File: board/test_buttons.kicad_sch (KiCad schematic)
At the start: 0 parts

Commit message: Added Parts, Renamed Parts
Added in switches, buttons, & multiple anderson connections for power.
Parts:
- added SW1, SW2, SW3: SW_Push, symbol Switch:SW_Push
- added SW4: SW_SPDT, symbol Switch:SW_SPDT
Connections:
- new net +3.3V: SW4.1 (A)
- new net Dir_Switch: SW4.2 (B)
- new net GND: SW1.2, SW2.2, SW3.2, SW4.3 (C)
- new net SW1: SW1.1
- new net SW2: SW2.1
- new net SW3: SW3.1

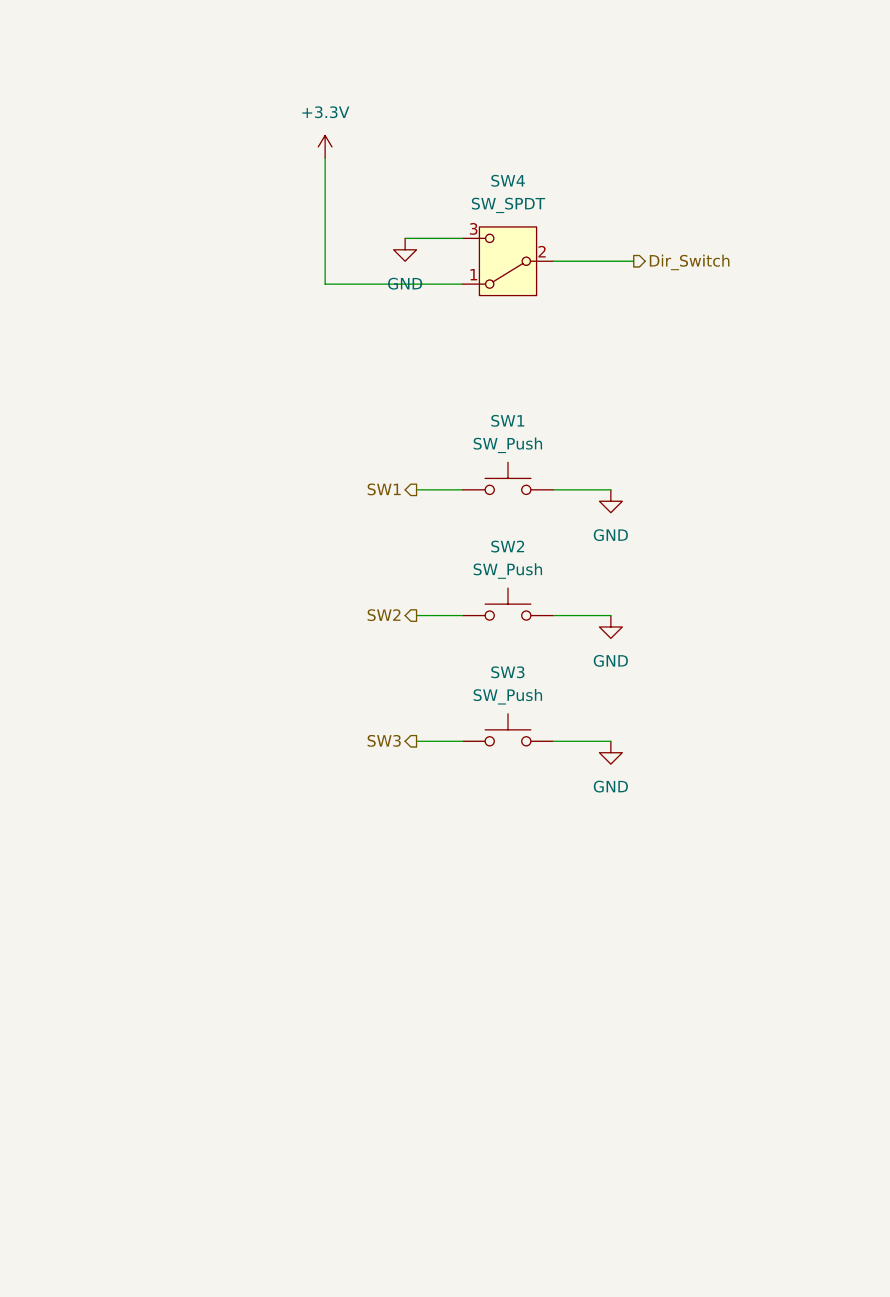
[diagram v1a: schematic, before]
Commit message: Added Labels, Missing Requirements, and Refined Look
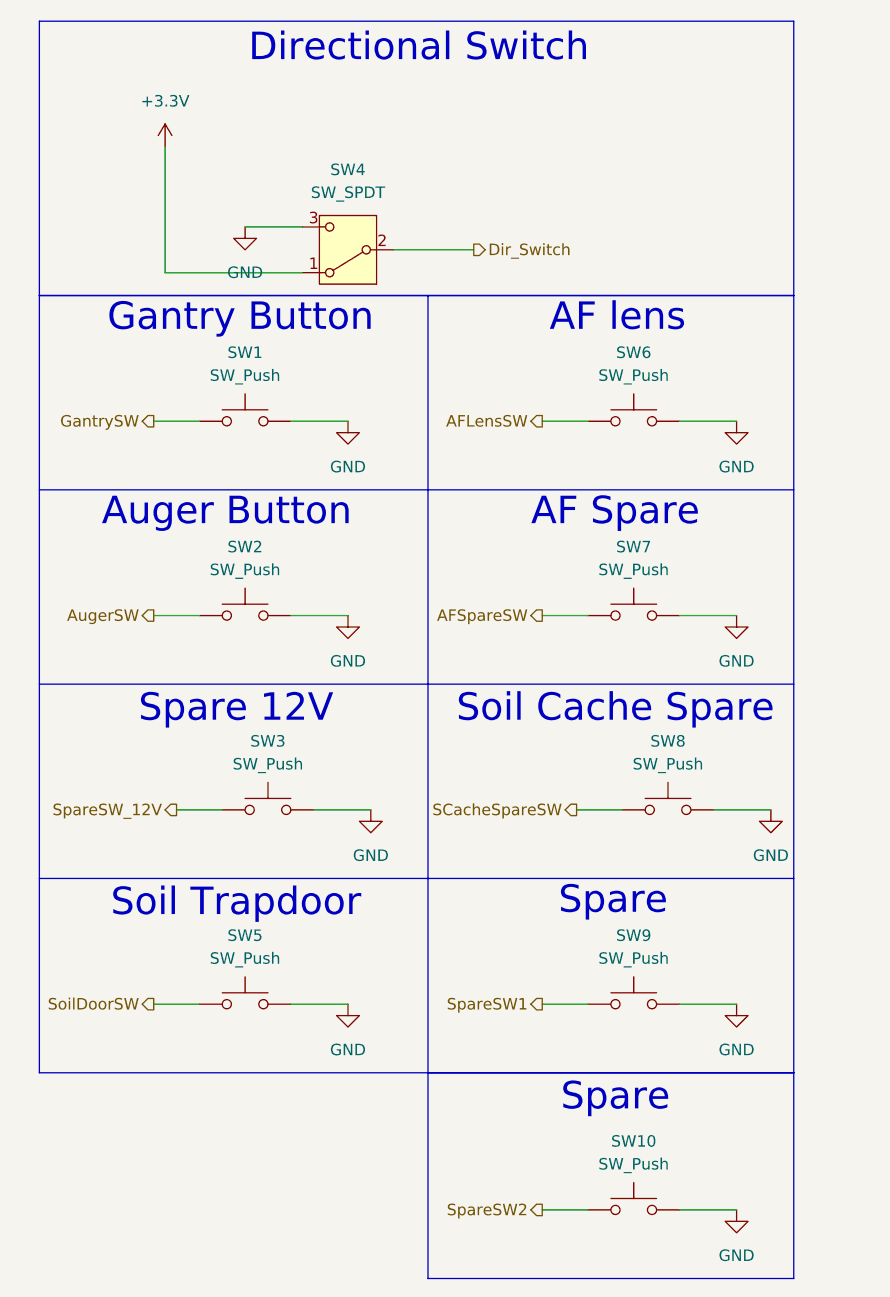
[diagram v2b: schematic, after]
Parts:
- added SW10, SW5, SW6, SW7, SW8, SW9: SW_Push, symbol Switch:SW_Push
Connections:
- net GND: now also SW10.2, SW5.2, SW6.2, SW7.2, SW8.2, SW9.2
- net SW1 renamed GantrySW
- net SW2 renamed AugerSW
- net SW3 renamed SpareSW_12V
- new net AFLensSW: SW6.1
- new net AFSpareSW: SW7.1
- new net SCacheSpareSW: SW8.1
- new net SoilDoorSW: SW5.1
- new net SpareSW1: SW9.1
- new net SpareSW2: SW10.1
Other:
- note added: "AF Spare"
- note added: "AF lens"
- note added: "Auger Button"
- note added: "Directional Switch"
- note added: "Gantry Button"
- note added: "Soil Cache Spare"
- note added: "Soil Trapdoor"
- note added: "Spare"
- note added: "Spare 12V"
- moved on the sheet: SW1, SW2, SW3, SW4

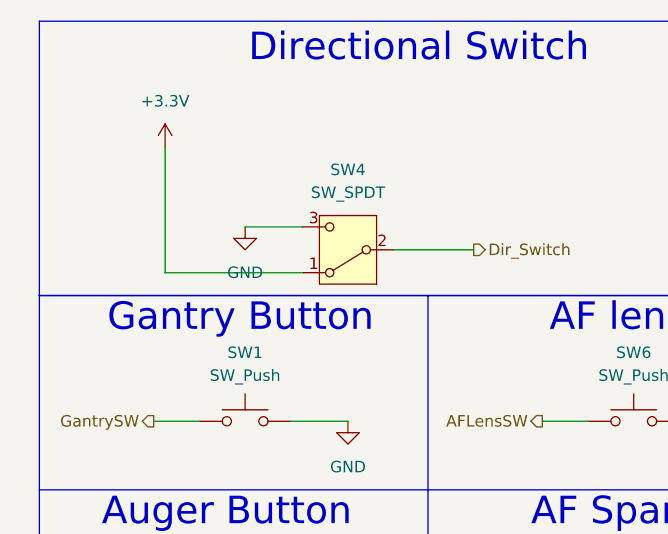
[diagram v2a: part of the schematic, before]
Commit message: Adjusted resistor values & renamed AF outputs
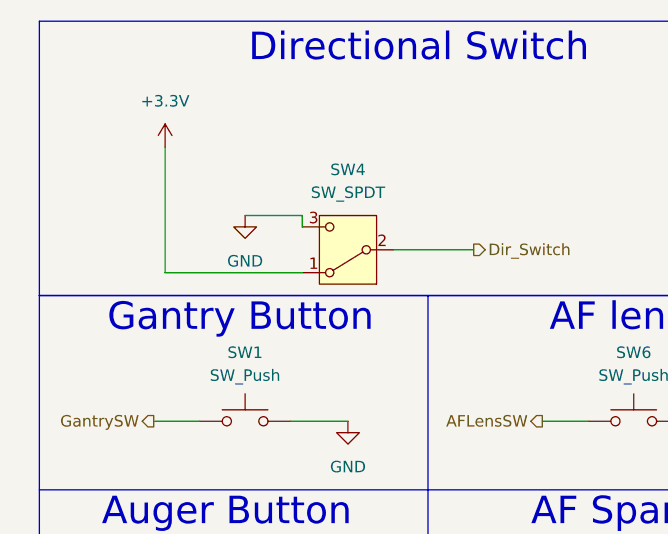
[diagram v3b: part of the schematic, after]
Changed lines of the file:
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@@
+	(wire
+		(pts
+			(xy 41.91 34.29) (xy 41.91 35.56)
+		)
+		(stroke
+			(width 0)
+			(type default)
+		)
+	)
 	(wire
 		(pts
@@
 	(wire
 		(pts
-			(xy 35.56 35.56) (xy 41.91 35.56)
+			(xy 35.56 34.29) (xy 41.91 34.29)
 		)
 		(stroke
@@
 	(symbol
 		(lib_id "power:GND")
-		(at 35.56 35.56 0)
+		(at 35.56 34.29 0)
 		(unit 1)
 		(exclude_from_sim no)
@@
 		(fields_autoplaced yes)
 		(property "Reference" "#PWR028"
-			(at 35.56 41.91 0)
+			(at 35.56 40.64 0)
 			(effects
 				(font
@@
 		)
 		(property "Value" "GND"
-			(at 35.56 40.64 0)
-			(effects
-				(font
-					(size 1.27 1.27)
-				)
-			)
-		)
-		(property "Footprint" ""
-			(at 35.56 35.56 0)
+			(at 35.56 39.37 0)
+			(effects
+				(font
+					(size 1.27 1.27)
+				)
+			)
+		)
+		(property "Footprint" ""
+			(at 35.56 34.29 0)
 			(effects
 				(font
@@
 		)
 		(property "Datasheet" ""
-			(at 35.56 35.56 0)
+			(at 35.56 34.29 0)
 			(effects
 				(font
@@
 		)
 		(property "Description" "Power symbol creates a global label with name \"GND\" , ground"
-			(at 35.56 35.56 0)
-			(effects
-				(font
+			(at 35.56 34.29 0)
+			(effects
+				(font

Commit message: assigned footprints
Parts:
- SW1, SW10, SW2, SW3, SW5, SW6, SW7, SW8, SW9: footprint (none) -> Button_Switch_SMD:SW_SPST_TL3305A
- SW4: footprint (none) -> Button_Switch_THT:SW_Slide_SPDT_Straight_CK_OS102011MS2Q
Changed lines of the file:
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@@
 			)
 		)
-		(property "Footprint" ""
+		(property "Footprint" "Button_Switch_SMD:SW_SPST_TL3305A"
 			(at 35.56 116.84 0)
 			(effects
@@
 			)
 		)
-		(property "Footprint" ""
+		(property "Footprint" "Button_Switch_SMD:SW_SPST_TL3305A"
 			(at 78.74 52.07 0)
 			(effects
@@
 			)
 		)
-		(property "Footprint" ""
+		(property "Footprint" "Button_Switch_SMD:SW_SPST_TL3305A"
 			(at 35.56 73.66 0)
 			(effects
@@
 			)
 		)
-		(property "Footprint" ""
+		(property "Footprint" "Button_Switch_SMD:SW_SPST_TL3305A"
 			(at 78.74 139.7 0)
 			(effects
@@
 			)
 		)
-		(property "Footprint" ""
+		(property "Footprint" "Button_Switch_SMD:SW_SPST_TL3305A"
 			(at 78.74 116.84 0)
 			(effects
@@
 			)
 		)
-		(property "Footprint" ""
+		(property "Footprint" "Button_Switch_SMD:SW_SPST_TL3305A"
 			(at 35.56 52.07 0)
 			(effects
@@
 			)
 		)
-		(property "Footprint" ""
+		(property "Footprint" "Button_Switch_SMD:SW_SPST_TL3305A"
 			(at 38.1 95.25 0)
 			(effects
@@
 			)
 		)
-		(property "Footprint" ""
+		(property "Footprint" "Button_Switch_THT:SW_Slide_SPDT_Straight_CK_OS102011MS2Q"
 			(at 46.99 38.1 0)
 			(effects
@@
 			)
 		)
-		(property "Footprint" ""
+		(property "Footprint" "Button_Switch_SMD:SW_SPST_TL3305A"
 			(at 78.74 73.66 0)
 			(effects
@@
 			)
 		)
-		(property "Footprint" ""
+		(property "Footprint" "Button_Switch_SMD:SW_SPST_TL3305A"
 			(at 82.55 95.25 0)
 			(effects

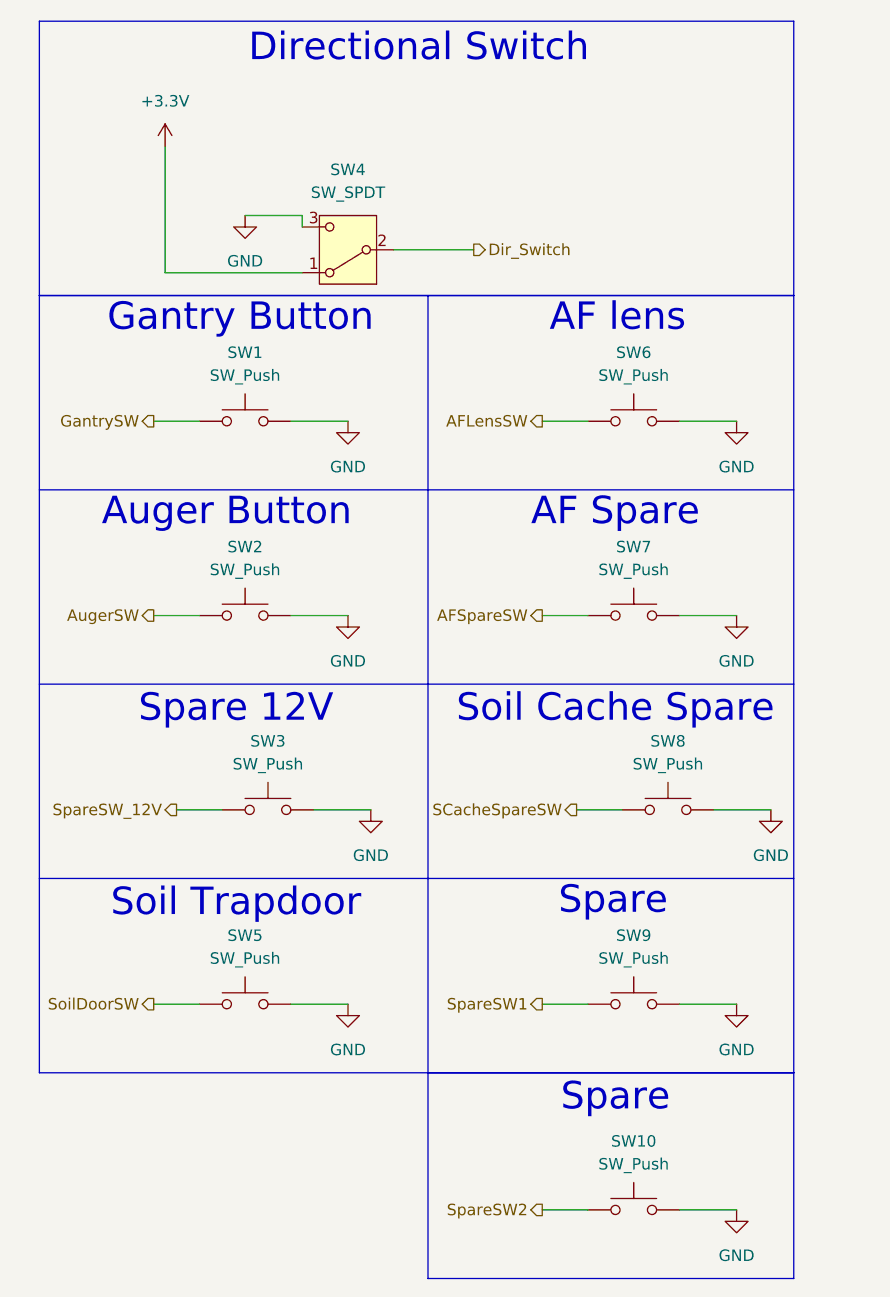
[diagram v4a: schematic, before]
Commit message: Fixed issues after schematic review
added 6 leds for every servo, changed txd and rxd to pins 30/31, added additional oki for 3.3V
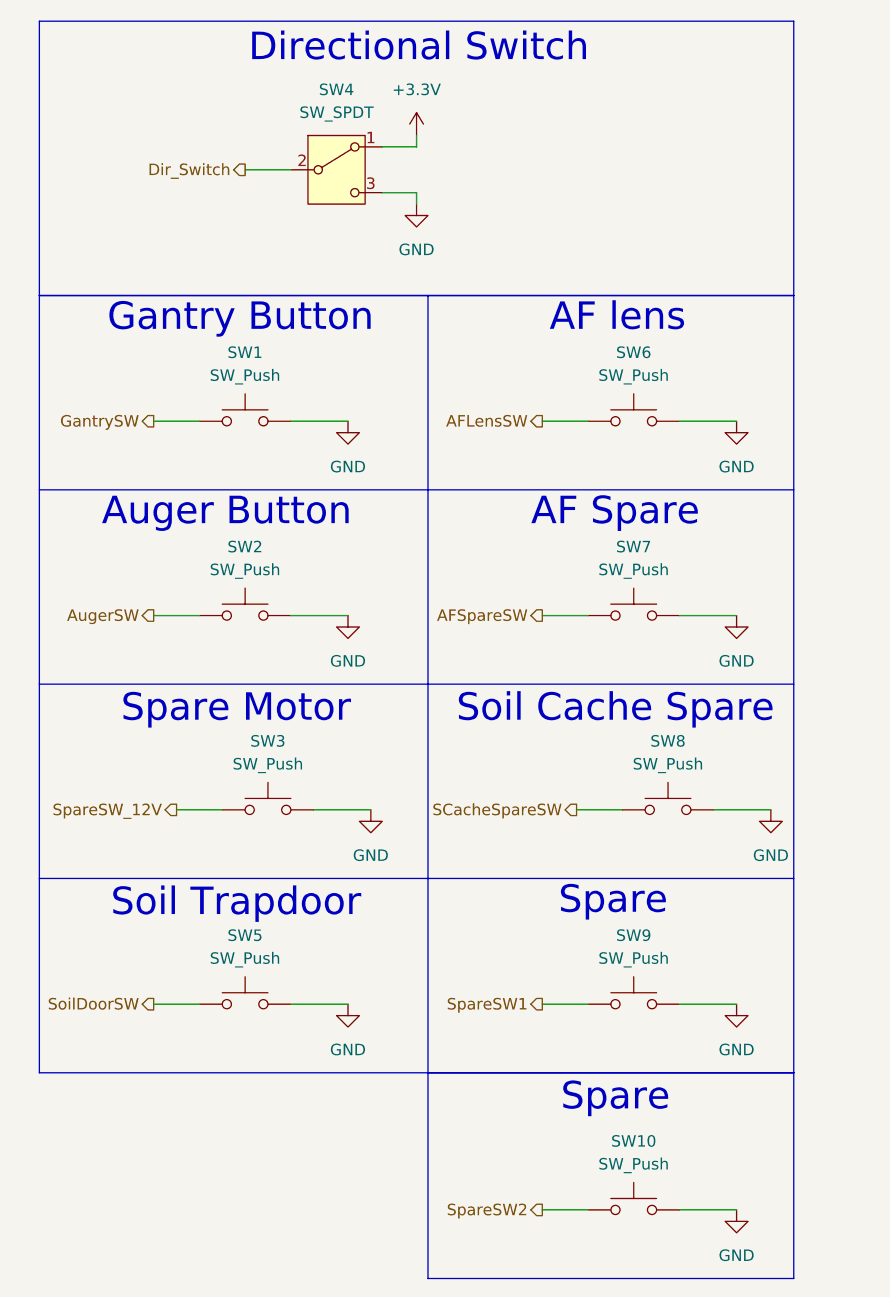
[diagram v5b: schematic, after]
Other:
- note added: "Spare Motor"
- note removed: "Spare 12V"
- moved on the sheet: SW4
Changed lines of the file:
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@@
 		)
 	)
-	(text "Spare 12V"
+	(text "Spare Motor"
 		(exclude_from_sim no)
 		(at 34.544 89.154 0)
@@
 	(wire
 		(pts
-			(xy 26.67 40.64) (xy 26.67 26.67)
-		)
-		(stroke
-			(width 0)
-			(type default)
-		)
-	)
-	(wire
-		(pts
-			(xy 41.91 40.64) (xy 26.67 40.64)
+			(xy 35.56 29.21) (xy 40.64 29.21)
 		)
 		(stroke
@@
 	(wire
 		(pts
+			(xy 54.61 25.4) (xy 54.61 26.67)
+		)
+		(stroke
+			(width 0)
+			(type default)
+		)
+	)
+	(wire
+		(pts
+			(xy 50.8 26.67) (xy 54.61 26.67)
+		)
+		(stroke
+			(width 0)
+			(type default)
+		)
+	)
+	(wire
+		(pts
 			(xy 83.82 144.78) (xy 90.17 144.78)
 		)
@@
 		)
 	)
+	(wire
+		(pts
+			(xy 50.8 31.75) (xy 54.61 31.75)
+		)
+		(stroke
+			(width 0)
+			(type default)
+		)
+	)
 	(polyline
 		(pts
@@
 	(wire
 		(pts
-			(xy 41.91 34.29) (xy 41.91 35.56)
-		)
-		(stroke
-			(width 0)
-			(type default)
-		)
-	)
-	(wire
-		(pts
-			(xy 52.07 38.1) (xy 60.96 38.1)
+			(xy 54.61 31.75) (xy 54.61 33.02)
 		)
 		(stroke
@@
 		(pts
 			(xy 25.4 57.15) (xy 30.48 57.15)
-		)
-		(stroke
-			(width 0)
-			(type default)
-		)
-	)
-	(wire
-		(pts
-			(xy 35.56 34.29) (xy 41.91 34.29)
 		)
 		(stroke
@@
 	(hierarchical_label "Dir_Switch"
 		(shape output)
-		(at 60.96 38.1 0)
+		(at 35.56 29.21 180)
 		(effects
 			(font
 				(size 1.27 1.27)
 			)
-			(justify left)
+			(justify right)
 		)
 	)
@@
 	(symbol
 		(lib_id "power:GND")
-		(at 35.56 34.29 0)
+		(at 54.61 33.02 0)
 		(unit 1)
 		(exclude_from_sim no)
@@
 		(fields_autoplaced yes)
 		(property "Reference" "#PWR028"
-			(at 35.56 40.64 0)
+			(at 54.61 39.37 0)
 			(effects
 				(font
@@
 		)
 		(property "Value" "GND"
-			(at 35.56 39.37 0)
+			(at 54.61 38.1 0)
 			(effects
 				(font
@@
 		)
 		(property "Footprint" ""
-			(at 35.56 34.29 0)
+			(at 54.61 33.02 0)
 			(effects
 				(font
@@
 		)
 		(property "Datasheet" ""
-			(at 35.56 34.29 0)
+			(at 54.61 33.02 0)
 			(effects
 				(font
@@
 		)
 		(property "Description" "Power symbol creates a global label with name \"GND\" , ground"
-			(at 35.56 34.29 0)
+			(at 54.61 33.02 0)
 			(effects
 				(font
@@
 	(symbol
 		(lib_id "power:+3.3V")
-		(at 26.67 26.67 0)
+		(at 54.61 25.4 0)
 		(unit 1)
 		(exclude_from_sim no)
@@
 		(fields_autoplaced yes)
 		(property "Reference" "#PWR029"
-			(at 26.67 30.48 0)
+			(at 54.61 29.21 0)
 			(effects
 				(font
@@
 		)
 		(property "Value" "+3.3V"
-			(at 26.67 21.59 0)
+			(at 54.61 20.32 0)
 			(effects
 				(font
@@
 		)
 		(property "Footprint" ""
-			(at 26.67 26.67 0)
+			(at 54.61 25.4 0)
 			(effects
 				(font
@@
 		)
 		(property "Datasheet" ""
-			(at 26.67 26.67 0)
+			(at 54.61 25.4 0)
 			(effects
 				(font
@@
 		)
 		(property "Description" "Power symbol creates a global label with name \"+3.3V\""
-			(at 26.67 26.67 0)
+			(at 54.61 25.4 0)
 			(effects
 				(font
@@
 	(symbol
 		(lib_id "Switch:SW_SPDT")
-		(at 46.99 38.1 180)
+		(at 45.72 29.21 0)
 		(unit 1)
 		(exclude_from_sim no)
@@
 		(fields_autoplaced yes)
 		(property "Reference" "SW4"
-			(at 46.99 29.21 0)
+			(at 45.72 20.32 0)
 			(effects
 				(font
@@
 		)
 		(property "Value" "SW_SPDT"
-			(at 46.99 31.75 0)
+			(at 45.72 22.86 0)
 			(effects
 				(font
@@
 		)
 		(property "Footprint" "Button_Switch_THT:SW_Slide_SPDT_Straight_CK_OS102011MS2Q"
-			(at 46.99 38.1 0)
+			(at 45.72 29.21 0)
 			(effects
 				(font
@@
 		)
 		(property "Datasheet" "~"
-			(at 46.99 30.48 0)
+			(at 45.72 36.83 0)
 			(effects
 				(font
@@
 		)
 		(property "Description" "Switch, single pole double throw"
-			(at 46.99 38.1 0)
-			(effects
-				(font
+			(at 45.72 29.21 0)
+			(effects
+				(font
